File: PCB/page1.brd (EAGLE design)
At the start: 100.3 x 48 mm, 15 parts, among them IC3 MEGA16-A

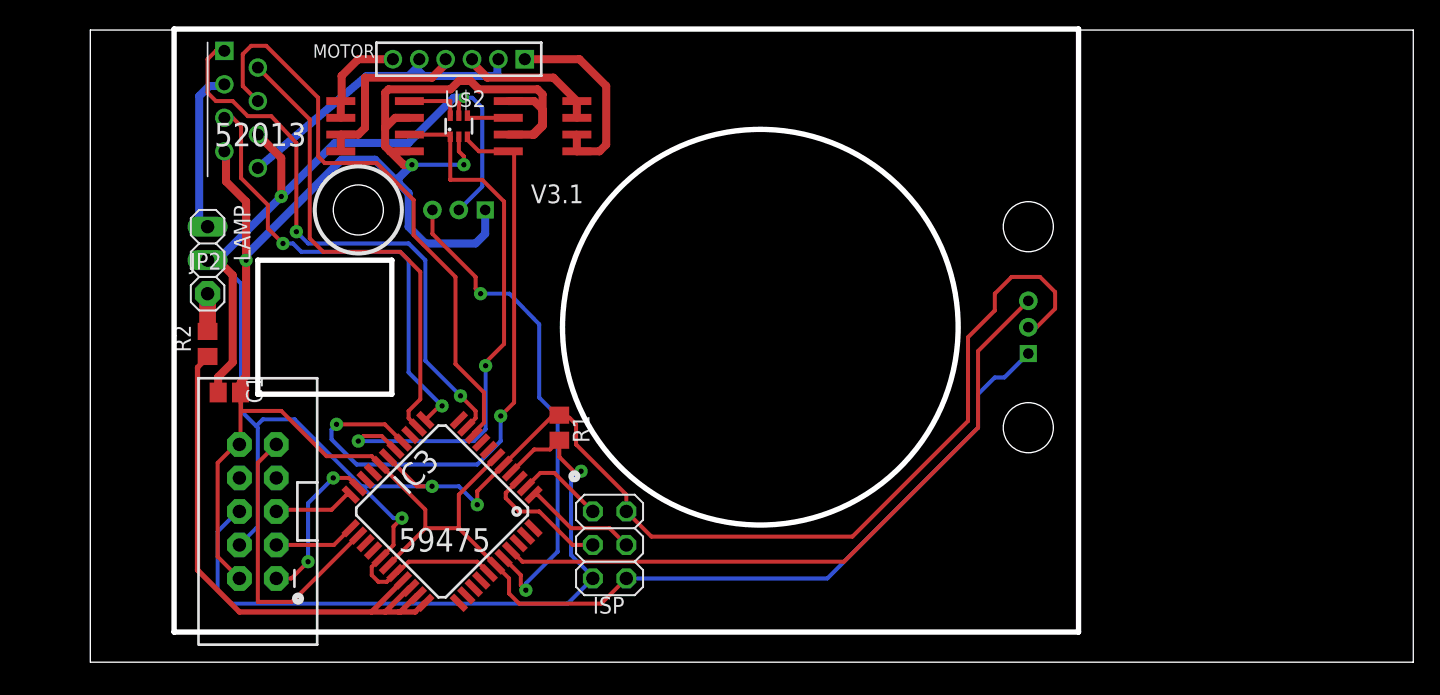
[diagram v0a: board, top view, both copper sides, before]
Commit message: updated to version 3.2 of led PCB
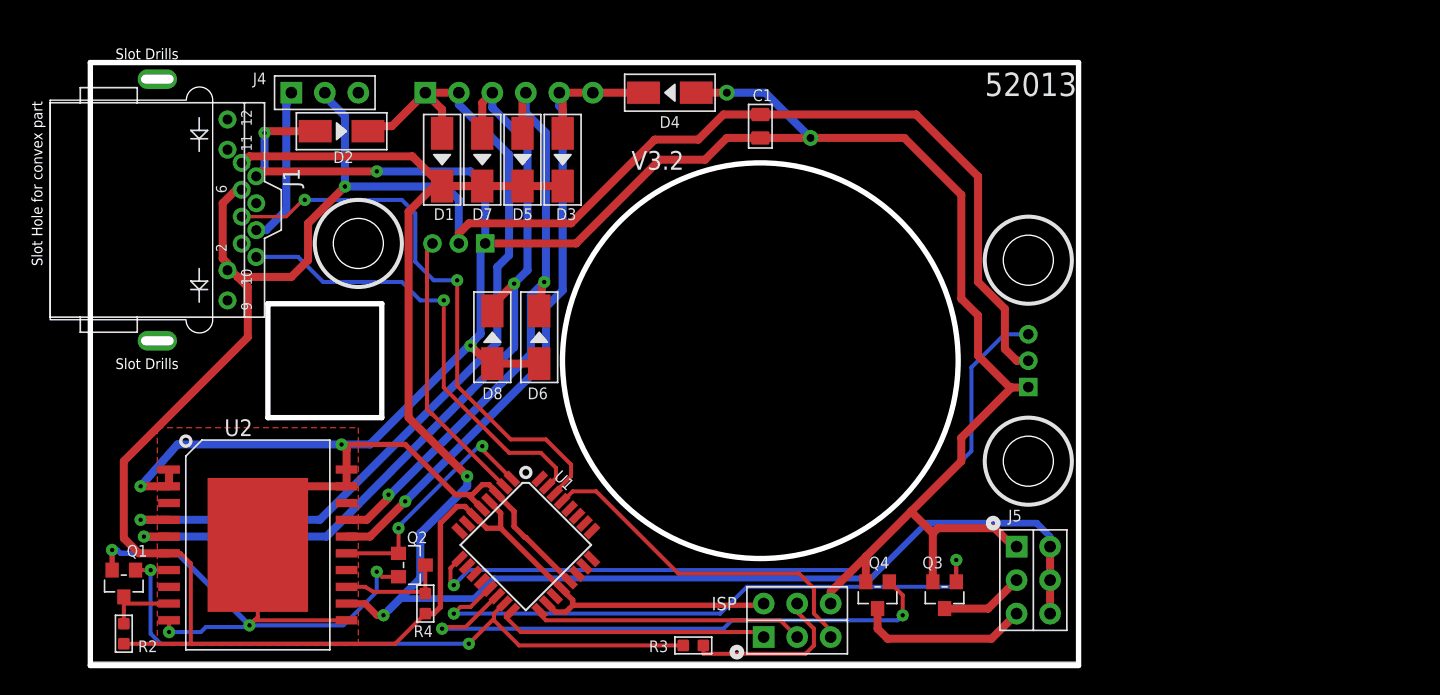
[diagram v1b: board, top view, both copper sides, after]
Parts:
- removed IC3: MEGA16-A, atmel:TQFP44
- removed JP1: M05X2SHD_LOCK, SparkFun-Connectors:2X5-SHROUDED_LOCK
- removed JP2: (no value), adafruit:1X01
- removed LAMP: (no value), pinhead:1X02
- removed MOTOR: (no value), pinhead-2:1X06M
- removed R1: 20k, rcl:R0805
- removed U$1: RJ-45-EDGE, Chris_parts:RJ-45-EDGE
- removed U$2: 742G04, Chris_parts:SOT363_PHILIPS
- removed U$3, U$4: N-FET_DUAL, Chris_parts:SO08
- added D1, D2, D3, D4, D5, D6, D7, D8: (no value), OPL Eagle Library:DO-214AC
- added J1: RJ45-MJ88-BX11-RVSL2-3420050P1, OPL Eagle Library:RJ45-MJ88-BX11-RVSL2
- added J2: CONNECTOR-HEADER-6P-3460650P1, OPL Eagle Library:1X6P-2.54-2.54-11.6-3.0-BLACK-MALE
- added J4: CONNECTOR-HEADER-3P-3460810P1, OPL Eagle Library:1X3P-2.54-2.54-11.6-3.0-BLACK-MALE
- added J5: CONNECTOR-HEADER-2X3P-3460180P1, OPL Eagle Library:2X3P-2.54-2.54-11.6-3.0-BLACK-MALE
- added Q1, Q2, Q3, Q4: MOSFET-N-044020001, OPL Eagle Library:SOT23
- added R3, R4: 10k, OPL Eagle Library:R0603
- added U1: ATMEGA328P-AU-1030060P1, OPL Eagle Library:TQFP32
- added U2: L298-1420010P1, OPL Eagle Library:POWERSO-20
- C1: value (none) -> 1uF; device rcl:C2012 -> OPL Eagle Library:C0805
- ISP: value (none) -> CONNECTOR-HEADER-2X3P-3460180P1; device pinhead:2X03 -> OPL Eagle Library:2X3P-2.54-2.54-11.6-3.0-BLACK-MALE
- R2: value 20k -> 10k; device rcl:R0805 -> OPL Eagle Library:R0603
- moved C1 45.0 mm to (50.8, 40.6), turned to 90 degrees
- moved R2 22.9 mm to (2.54, 2.16)
- moved ISP 15.3 mm to (53.6, 3.17), turned to 90 degrees
- moved U$5 2.54 mm to (27.9, 31.8)
- moved U$6 2.54 mm to (71.1, 22.9)
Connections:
- removed net LED-: LAMP.2, U$1.3
- removed net N$2: U$2.6, U$3.4
- removed net N$6: MOTOR.1, U$4.5, U$4.6
- removed net N$7: MOTOR.3, U$4.7, U$4.8
- removed net N$8: MOTOR.4, U$3.7, U$3.8
- removed net N$9: MOTOR.6, U$3.5, U$3.6
- removed net TCK: IC3.21, JP1.1
- removed net TDI: IC3.24, JP1.9
- removed net TDO: IC3.23, JP1.3
- removed net TMS: IC3.22, JP1.5
- new net !A: Q1.3, R2.2, U2.9
- new net !B: Q2.3, R4.2, U2.13
- new net ENA: U2.8
- new net ENB: U2.14
- new net M1!A: D7.1, D8.2, J2.3, U2.5
- new net M1!B: D3.1, D4.2, J2.5, J2.6, U2.16
- new net M1A: D1.1, D2.2, J2.1, J2.2, U2.4
- new net M1B: D5.1, D6.2, J2.4, U2.17
- new net PB1: Q3.1, U1.13
- new net PB2: Q4.1, U1.14
- net +12V: now also D1.2, D3.2, D5.2, D7.2, J1.8, J5.4, J5.5, J5.6, U2.12; no longer MOTOR.2, MOTOR.5, U$1.8
- net +5V: now also C1.2, ISP.6, J1.10, J1.6, J4.2, R2.1, R4.1, U1.18, U1.20, U1.4, U1.6, U2.6; no longer C1.1, IC3.17, IC3.27, IC3.29, IC3.38, IC3.5, ISP.2, JP1.4, LAMP.1, R1.2, U$1.6, U$2.5
- net GND: now also C1.1, D2.1, D4.1, D6.1, D8.1, ISP.4, J1.7, J5.1, Q1.2, Q2.2, Q3.2, Q4.2, U1.21, U1.3, U1.5, U2.1, U2.10, U2.11, U2.19, U2.2, U2.20, U2.THERMALS; no longer C1.2, IC3.18, IC3.28, IC3.39, IC3.6, ISP.6, JP1.10, JP1.2, U$1.7, U$2.2, U$3.1, U$3.3, U$4.1, U$4.3
- net LF1: now also U1.2; no longer IC3.40
- net LF2: now also U1.9; no longer IC3.41
- net MISO: now also U1.16; no longer IC3.2
- net MOSI: now also ISP.5, R3.1; no longer IC3.1, ISP.4
- net N$1: now also J1.3, J4.1; no longer U$2.4, U$4.2
- net N$3: now also J5.3, Q4.3; no longer JP2.1, R2.2
- net N$4: now also J5.2, Q3.3; no longer IC3.30, IC3.31, IC3.32, IC3.33, R2.1
- net NC1: now also J1.2; no longer IC3.13, U$1.2
- net NC2: now also J1.5; no longer IC3.12, U$1.5
- net OSC2A: now also Q1.1, R3.2, U1.15, U2.7; no longer IC3.15, U$2.3, U$4.4
- net OSC2B: now also Q2.1, U1.1, U2.15; no longer IC3.16, U$2.1, U$3.2
- net RST: now also ISP.3, U1.29; no longer IC3.4, ISP.5, JP1.6, R1.1
- net SCK: now also ISP.2, U1.17; no longer IC3.3, ISP.3
- net S_RX: now also J1.4, U1.30; no longer IC3.9, U$1.4
- net S_TX: now also J1.1, U1.31; no longer IC3.10, U$1.1
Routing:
- net +12V: track 23.3 -> 129.3 mm, vias 0 -> 2
- net GND: track 192.4 -> 269.9 mm, vias 3 -> 11
- net M1A: track 0.00 -> 67.4 mm, vias 0 -> 1
- net M1!A: track 0.00 -> 62.9 mm, vias 0 -> 2
- net M1!B: track 0.00 -> 51.2 mm, vias 0 -> 1
- net PB1: track 0.00 -> 45.9 mm, vias 0 -> 2
- net M1B: track 0.00 -> 45.7 mm, vias 0 -> 2
- net PB2: track 0.00 -> 43.5 mm, vias 0 -> 2
- net N$4: track 43.3 -> 6.36 mm
- net NC1: track 36.5 -> 0.00 mm
- net NC2: track 35.6 -> 0.00 mm, vias 2 -> 0
- net RST: track 53.5 -> 26.7 mm, vias 1 -> 0
- net OSC2B: track 42.5 -> 18.2 mm
- net TDI: track 22.2 -> 0.00 mm
- net LF1: track 38.2 -> 21.0 mm, vias 2 -> 0
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- added copper zone on layer 1, net GND
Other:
- board size 100.3 x 48 mm -> 74.9 x 45.7 mm
- board text added: "V3.2"
- board text removed: "59475"
- board text removed: "V3.1"

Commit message: Updated PCB design for ledboard 3.2r1
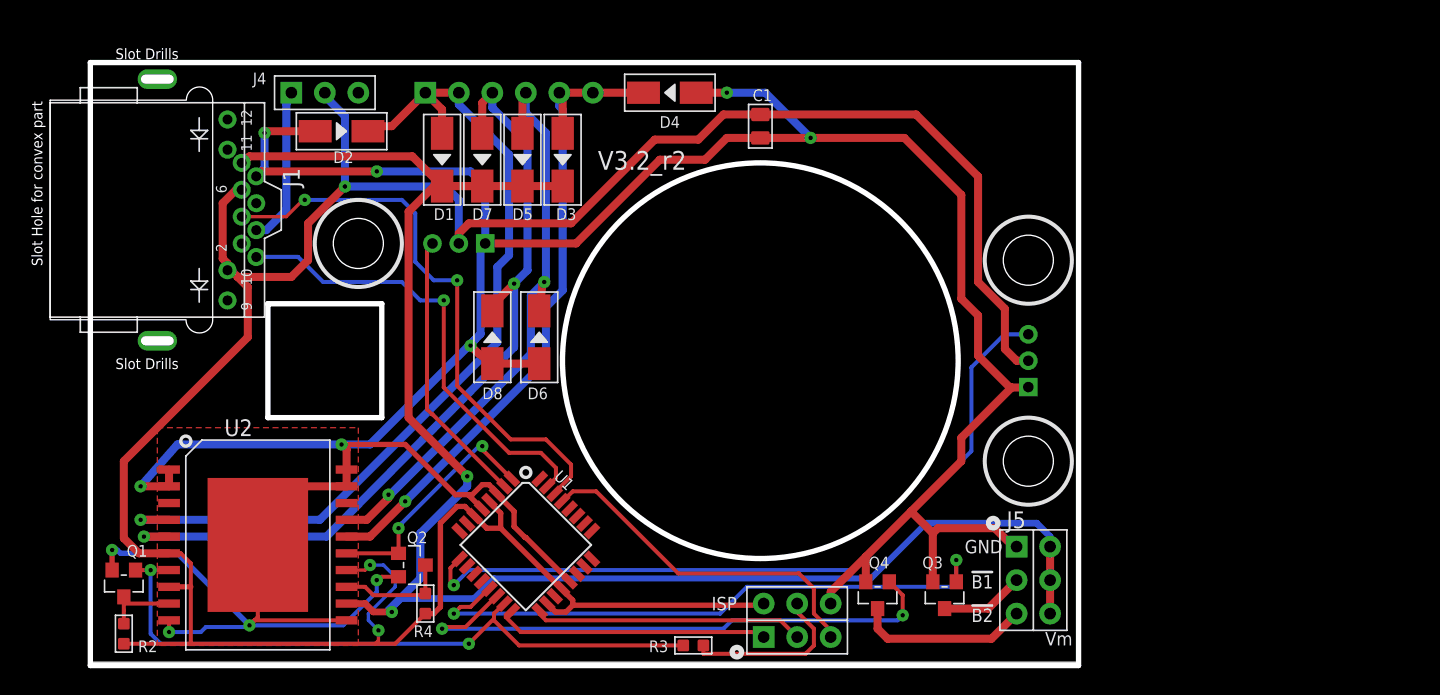
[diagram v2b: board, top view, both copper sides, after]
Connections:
- removed net ENA: U2.8
- removed net ENB: U2.14
- net +5V: now also U2.14, U2.8
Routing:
- net +5V: track 203.7 -> 215.9 mm, vias 1 -> 3
- net GND: track 269.9 -> 269.2 mm
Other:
- board text added: "!B1"
- board text added: "!B2"
- board text added: "GND"
- board text added: "V3.2_r2"
- board text added: "Vm"
- board text removed: "52013"
- board text removed: "V3.2"
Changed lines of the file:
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@@
 <wire x1="74.93" y1="45.466" x2="0" y2="45.466" width="0.4064" layer="46"/>
 <wire x1="0" y1="45.466" x2="0" y2="-0.254" width="0.4064" layer="46"/>
-<text x="67.818" y="42.926" size="1.778" layer="25">52013</text>
 <hole x="20.32" y="31.75" drill="3.7972"/>
 <hole x="71.12" y="30.48" drill="3.7972"/>
 <hole x="71.12" y="15.24" drill="3.7972"/>
-<text x="41.021" y="37.338" size="1.4224" layer="21" font="vector" ratio="15">V3.2</text>
+<text x="38.481" y="37.338" size="1.4224" layer="21" font="vector" ratio="15">V3.2_r2</text>
 <circle x="50.8" y="22.86" radius="15" width="0.4064" layer="46"/>
 <wire x1="22.098" y1="27.178" x2="13.462" y2="27.178" width="0.4064" layer="46"/>
@@
 <circle x="49.022" y="0.762" radius="0.359209375" width="0.4064" layer="25"/>
 <circle x="68.453" y="10.541" radius="0.359209375" width="0.4064" layer="25"/>
+<text x="66.802" y="5.588" size="1.016" layer="25" font="vector" ratio="20">!B1</text>
+<text x="66.802" y="3.048" size="1.016" layer="25" font="vector" ratio="20">!B2</text>
+<text x="72.39" y="1.27" size="1.016" layer="25" font="vector" ratio="20">Vm</text>
+<text x="66.294" y="8.255" size="1.016" layer="25" font="vector" ratio="20">GND</text>
 </plain>
 <attributes>
@@
 </element>
 <element name="J5" library="OPL Eagle Library" package="2X3P-2.54-2.54-11.6-3.0-BLACK-MALE" value="CONNECTOR-HEADER-2X3P-3460180P1" x="71.501" y="6.223" smashed="yes">
-<attribute name="NAME" x="69.596" y="10.668" size="0.889" layer="25" font="vector" ratio="20"/>
+<attribute name="NAME" x="69.469" y="10.16" size="1.27" layer="25" font="vector" ratio="20"/>
 <attribute name="VALUE" x="72.136" y="4.318" size="0.635" layer="27" ratio="10" rot="R90"/>
 </element>
@@
 <wire x1="29.083" y1="4.826" x2="23.495" y2="4.826" width="0.508" layer="16"/>
 <wire x1="23.495" y1="4.826" x2="22.606" y2="3.937" width="0.508" layer="16"/>
-<via x="22.225" y="3.556" extent="1-16" drill="0.3302"/>
-<wire x1="22.606" y1="3.937" x2="22.225" y2="3.556" width="0.508" layer="16"/>
-<wire x1="22.225" y1="3.556" x2="21.717" y2="3.556" width="0.508" layer="1"/>
-<wire x1="21.717" y1="3.556" x2="20.828" y2="4.445" width="0.508" layer="1"/>
+<via x="22.86" y="3.81" extent="1-16" drill="0.3302"/>
+<wire x1="22.606" y1="3.937" x2="22.86" y2="3.81" width="0.508" layer="16"/>
+<wire x1="22.86" y1="3.81" x2="21.463" y2="3.81" width="0.508" layer="1"/>
+<wire x1="21.463" y1="3.81" x2="20.828" y2="4.445" width="0.508" layer="1"/>
 <wire x1="20.828" y1="4.445" x2="19.431" y2="4.445" width="0.508" layer="1"/>
 <wire x1="11.48" y1="37.86" x2="11.571" y2="37.86" width="0.6096" layer="1"/>
@@
 <wire x1="30.8332" y1="12.773853125" x2="30.914146875" y2="12.773853125" width="0.4064" layer="1"/>
 <wire x1="23.368" y1="6.477" x2="22.098" y2="6.477" width="0.3048" layer="1"/>
-<wire x1="22.098" y1="6.477" x2="21.717" y2="6.858" width="0.3048" layer="1"/>
-<via x="21.717" y="6.858" extent="1-16" drill="0.3302"/>
-<wire x1="21.717" y1="6.858" x2="21.717" y2="5.334" width="0.3048" layer="16"/>
+<wire x1="22.098" y1="6.477" x2="21.717" y2="6.223" width="0.3048" layer="1"/>
+<via x="21.717" y="6.223" extent="1-16" drill="0.3302"/>
+<wire x1="21.717" y1="6.223" x2="21.717" y2="5.334" width="0.3048" layer="16"/>
 <wire x1="21.717" y1="5.334" x2="19.177" y2="2.794" width="0.3048" layer="16"/>
 <wire x1="19.431" y1="3.175" x2="12.446" y2="3.175" width="0.3048" layer="1"/>
@@
 <wire x1="13.208" y1="37.468" x2="12.58" y2="36.84" width="0.6096" layer="16"/>
 <wire x1="45.942" y1="43.18" x2="48.26" y2="43.18" width="0.6096" layer="1"/>
-<via x="48.26" y="43.18" extent="1-16" drill="0.6"/>
+<via x="48.26" y="43.18" extent="1-16" drill="0.3302"/>
 <wire x1="48.26" y1="43.18" x2="51.181" y2="43.18" width="0.6096" layer="16"/>
 <wire x1="51.181" y1="43.18" x2="54.61" y2="39.751" width="0.6096" layer="16"/>
-<via x="54.61" y="39.751" extent="1-16" drill="0.6"/>
+<via x="54.61" y="39.751" extent="1-16" drill="0.3302"/>
 <wire x1="30.48" y1="22.638" x2="29.432" y2="23.4" width="0.6096" layer="1"/>
 <wire x1="29.432" y1="23.4" x2="28.829" y2="24.003" width="0.6096" layer="1"/>
@@
 <wire x1="10.4" y1="30.24" x2="10.4" y2="29.72" width="0.6096" layer="1"/>
 <wire x1="25.4" y1="3.683" x2="23.114" y2="1.397" width="0.3048" layer="1"/>
-<wire x1="23.114" y1="1.397" x2="7.62" y2="1.397" width="0.3048" layer="1"/>
+<wire x1="23.114" y1="1.397" x2="21.59" y2="1.397" width="0.3048" layer="1"/>
+<wire x1="21.59" y1="1.397" x2="7.62" y2="1.397" width="0.3048" layer="1"/>
 <wire x1="7.62" y1="1.397" x2="2.54" y2="1.397" width="0.3048" layer="1"/>
 <wire x1="29.13614375" y1="11.076796875" x2="30.052940625" y2="10.16" width="0.4064" layer="1"/>
@@
 <wire x1="34.6411125" y1="4.440459375" x2="35.271571875" y2="3.81" width="0.4064" layer="1"/>
 <wire x1="35.271571875" y1="3.81" x2="36.068" y2="3.81" width="0.4064" layer="1"/>
-<wire x1="36.068" y1="3.81" x2="36.195" y2="3.937" width="0.4064" layer="1"/>
 <wire x1="36.576" y1="4.318" x2="36.576" y2="4.699" width="0.4064" layer="1"/>
 <wire x1="36.576" y1="4.699" x2="35.77248125" y2="5.50251875" width="0.4064" layer="1"/>
@@
 <wire x1="30.267515625" y1="12.20816875" x2="30.20983125" y2="12.20816875" width="0.4064" layer="1"/>
 <wire x1="6.858" y1="8.255" x2="7.62" y2="7.493" width="0.3048" layer="1"/>
-<wire x1="7.62" y1="7.493" x2="7.62" y2="1.397" width="0.3048" layer="1"/>
+<wire x1="7.62" y1="7.493" x2="7.62" y2="5.715" width="0.3048" layer="1"/>
+<wire x1="7.62" y1="5.715" x2="7.62" y2="1.397" width="0.3048" layer="1"/>
 <wire x1="10.666" y1="29.72" x2="10.4" y2="29.72" width="0.3048" layer="1"/>
 <wire x1="6.858" y1="8.255" x2="5.969" y2="8.255" width="0.3048" layer="1"/>
@@
 <wire x1="31.115" y1="11.303" x2="31.115" y2="10.16" width="0.4064" layer="1"/>
 <wire x1="50.927" y1="4.318" x2="36.576" y2="4.318" width="0.4064" layer="1"/>
-<wire x1="36.576" y1="4.318" x2="36.322" y2="4.064" width="0.4064" layer="1"/>
-<wire x1="36.322" y1="4.064" x2="36.195" y2="3.937" width="0.4064" layer="1"/>
+<wire x1="36.576" y1="4.318" x2="36.068" y2="3.81" width="0.4064" layer="1"/>
 <wire x1="29.13614375" y1="11.076796875" x2="28.401940625" y2="11.811" width="0.4064" layer="1"/>
 <wire x1="28.401940625" y1="11.811" x2="27.813" y2="11.811" width="0.4064" layer="1"/>
@@
 <wire x1="46.101" y1="39.624" x2="48.006" y2="41.529" width="0.6096" layer="1"/>
 <wire x1="48.006" y1="41.529" x2="50.8" y2="41.529" width="0.6096" layer="1"/>
+<contactref element="U2" pad="8"/>
+<contactref element="U2" pad="14"/>
+<wire x1="5.969" y1="5.715" x2="7.62" y2="5.715" width="0.4064" layer="1"/>
+<wire x1="19.431" y1="6.985" x2="20.828" y2="6.985" width="0.254" layer="1"/>
+<wire x1="20.828" y1="6.985" x2="21.209" y2="7.366" width="0.254" layer="1"/>
+<via x="21.209" y="7.366" extent="1-16" drill="0.3302"/>
+<wire x1="21.209" y1="7.366" x2="22.225" y2="7.366" width="0.254" layer="16"/>
+<wire x1="22.225" y1="7.366" x2="23.114" y2="6.477" width="0.254" layer="16"/>
+<wire x1="23.114" y1="6.477" x2="23.114" y2="5.715" width="0.254" layer="16"/>
+<wire x1="23.114" y1="5.715" x2="21.082" y2="3.683" width="0.254" layer="16"/>
+<wire x1="21.082" y1="3.683" x2="21.082" y2="3.175" width="0.254" layer="16"/>
+<wire x1="21.082" y1="3.175" x2="21.844" y2="2.413" width="0.254" layer="16"/>
+<via x="21.844" y="2.413" extent="1-16" drill="0.3302"/>
+<wire x1="21.844" y1="2.413" x2="21.844" y2="1.651" width="0.254" layer="1"/>
+<wire x1="21.844" y1="1.651" x2="21.59" y2="1.397" width="0.254" layer="1"/>
 </signal>
 <signal name="S_RX">
@@
 <wire x1="25.4" y1="5.207" x2="25.4" y2="7.366" width="0.3048" layer="1"/>
 <wire x1="19.431" y1="5.715" x2="20.828" y2="5.715" width="0.3048" layer="1"/>
-<wire x1="20.828" y1="5.715" x2="21.463" y2="5.334" width="0.3048" layer="1"/>
-<wire x1="21.463" y1="5.334" x2="25.019" y2="5.334" width="0.3048" layer="1"/>
-<wire x1="25.019" y1="5.334" x2="25.4" y2="5.207" width="0.3048" layer="1"/>
-</signal>
-<signal name="ENA">
-<contactref element="U2" pad="8"/>
-</signal>
-<signal name="ENB">
-<contactref element="U2" pad="14"/>
+<wire x1="20.828" y1="5.715" x2="21.463" y2="5.08" width="0.3048" layer="1"/>
+<wire x1="21.463" y1="5.08" x2="25.019" y2="5.08" width="0.3048" layer="1"/>
+<wire x1="25.019" y1="5.08" x2="25.4" y2="5.207" width="0.3048" layer="1"/>
 </signal>
 <signal name="M1A">
